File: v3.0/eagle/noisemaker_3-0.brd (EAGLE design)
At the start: 76.3 x 66.7 mm, 58 parts, among them IC1 REG1117, U3 ATMEGA32U4, Y1 16MHz

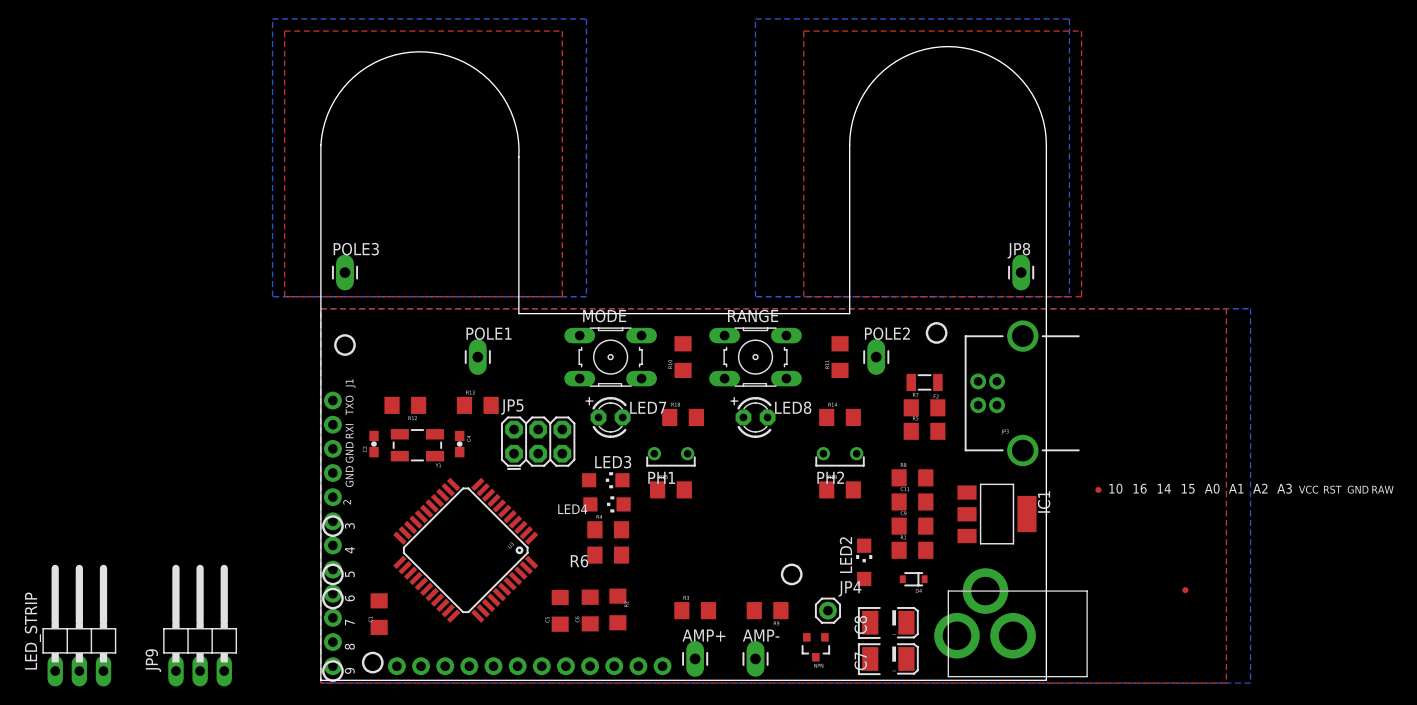
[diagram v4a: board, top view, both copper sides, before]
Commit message: board file
text has been updated, layout is completed. needs logos, names, more text love.
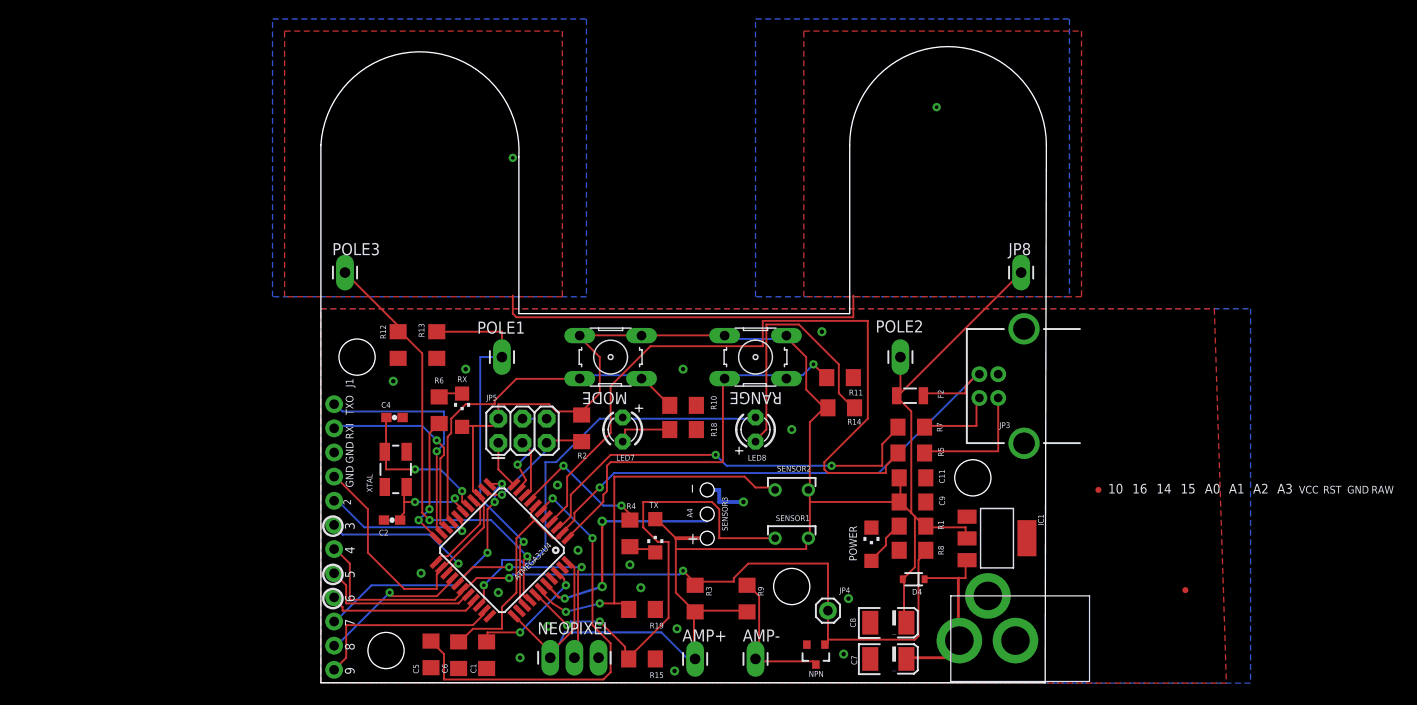
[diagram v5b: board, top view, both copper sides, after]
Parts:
- removed JP6: (no value), SparkFun:1X12
- removed JP9, LED_STRIP: (no value), pinhead:1X03/90
- removed LED2: Red, adafruit:CHIPLED_1206
- removed LED3: Yellow, adafruit:CHIPLED_1206
- removed LED4: Green, adafruit:CHIPLED_1206
- removed PH1, PH2: M9960_11B, photo-elements:M9960
- removed U3: ATMEGA32U4, SparkFun-DigitalIC:SPARKFUN-DIGITALIC_TQFP44
- removed Y1: 16MHz, SparkFun:CRYSTAL-SMD-5X3
- added ATMEGA32U4: ATMEGA32U4, SparkFun-DigitalIC:SPARKFUN-DIGITALIC_TQFP44
- added NEOPIXEL: (no value), SparkFun-Connectors:1X03_LONGPADS
- added POWER: Red, adafruit:CHIPLED_1206
- added RX: Green, adafruit:CHIPLED_1206
- added SENS3: (no value), SparkFun-Connectors:1X03_PP_HOLES_ONLY
- added SENSOR1, SENSOR2: M9960_11B, photo-elements:M9960
- added TX: Yellow, adafruit:CHIPLED_1206
- added XTAL: 16MHz, SparkFun:CRYSTAL-SMD-5X3
- moved R19 24.3 mm to (33.8, 7.75), turned to 180 degrees
- moved R6 23.4 mm to (12.4, 28.7), turned to 90 degrees
- moved R2 19.4 mm to (27.4, 26.8), turned to 90 degrees
- moved R15 18.0 mm to (33.8, 2.54), turned to 180 degrees
- moved C6 14.6 mm to (14.5, 2.94)
- moved C5 14.3 mm to (11.6, 3.02)
- moved C1 12.1 mm to (17.4, 2.94)
- moved C2 8.22 mm to (7.49, 17.1), turned to 180 degrees
- moved R13 7.68 mm to (12.2, 35.6), turned to 270 degrees
- moved R8 7.62 mm to (62.2, 14.0)
- moved C4 7.41 mm to (7.75, 27.9), turned to 0 degrees
- moved R12 6.40 mm to (8.13, 35.6), turned to 90 degrees
- moved R10 5.08 mm to (38.1, 29.2), turned to 180 degrees
- moved R5 2.68 mm to (62.1, 24.2)
- moved IC1 2.54 mm to (71.1, 15.2)
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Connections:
- removed net N$11: LED_STRIP.3
- removed net N$6: LED_STRIP.1
- net A0: now also ATMEGA32U4.36; no longer JP6.8, U3.36
- net A1: now also ATMEGA32U4.37; no longer JP6.7, U3.37
- net A2: now also ATMEGA32U4.38, SENSOR1.2; no longer JP6.6, PH1.2, U3.38
- net A3: now also ATMEGA32U4.39, SENSOR2.2; no longer JP6.5, PH2.2, U3.39
- net A4: now also ATMEGA32U4.40, SENS3.2; no longer JP9.2, U3.40
- net A5: now also ATMEGA32U4.41; no longer U3.41
- net AREF: now also ATMEGA32U4.42; no longer U3.42
- net D+: now also ATMEGA32U4.4; no longer U3.4
- net D-: now also ATMEGA32U4.3; no longer U3.3
- net D10: now also ATMEGA32U4.30, JP7.4; no longer JP6.12, U3.30
- net D11: now also ATMEGA32U4.12, JP7.3; no longer U3.12
- net D12: now also ATMEGA32U4.26, JP7.2; no longer U3.26
- net D13: now also ATMEGA32U4.32, JP7.1; no longer U3.32
- net D14: now also ATMEGA32U4.8; no longer U3.8
- net D2: now also ATMEGA32U4.19; no longer JP7.8, U3.19
- net D3: now also ATMEGA32U4.18, JP7.8; no longer JP7.7, U3.18
- net D4: now also ATMEGA32U4.25, JP7.7; no longer JP7.6, R11.2, RANGE.3, RANGE.4, U3.25
- net D5: now also ATMEGA32U4.31, LED7.A, LED8.K; no longer JP7.5, U3.31
- net D6: now also ATMEGA32U4.27, NEOPIXEL.2; no longer JP7.4, LED_STRIP.2, U3.27
- net D7: now also ATMEGA32U4.1, R11.2, RANGE.3, RANGE.4; no longer JP7.3, LED7.A, LED8.K, U3.1
- net D8: now also ATMEGA32U4.28, JP7.6; no longer JP7.2, U3.28
- net D9: now also ATMEGA32U4.29, JP7.5; no longer JP7.1, U3.29
- net GND: now also ATMEGA32U4.15, ATMEGA32U4.23, ATMEGA32U4.33, ATMEGA32U4.35, ATMEGA32U4.43, ATMEGA32U4.5, NEOPIXEL.3, POWER.C, SENS3.3; no longer JP6.2, JP7.9, JP9.3, LED2.C, U3.15, U3.23, U3.33, U3.35, U3.43, U3.5
- net MISO: now also ATMEGA32U4.11; no longer JP6.10, U3.11
- net MOSI: now also ATMEGA32U4.10; no longer JP6.11, U3.10
- net N$1: now also ATMEGA32U4.16, XTAL.1; no longer U3.16, Y1.1
- net N$10: now also POWER.A; no longer LED2.A
- net N$2: now also ATMEGA32U4.17, XTAL.3; no longer U3.17, Y1.3
- net N$4: now also ATMEGA32U4.6; no longer U3.6
- net N$5: now also TX.C; no longer LED3.C
- net N$7: now also RX.C; no longer LED4.C
- net RAW: no longer JP6.1
- net RESET: now also ATMEGA32U4.13; no longer JP6.3, U3.13
- net RXI: now also ATMEGA32U4.20; no longer U3.20
- net SCK: now also ATMEGA32U4.9; no longer JP6.9, U3.9
- net TXLED: now also ATMEGA32U4.22; no longer U3.22
- net TXO: now also ATMEGA32U4.21; no longer U3.21
- net UVCC: now also ATMEGA32U4.2, ATMEGA32U4.7; no longer U3.2, U3.7
- net VCC: now also ATMEGA32U4.14, ATMEGA32U4.24, ATMEGA32U4.34, ATMEGA32U4.44, JP7.9, NEOPIXEL.1, RX.A, SENS3.1, SENSOR1.1, SENSOR2.1, TX.A; no longer JP6.4, JP9.1, LED3.A, LED4.A, PH1.1, PH2.1, U3.14, U3.24, U3.34, U3.44
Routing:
- net VCC: track 0.00 -> 255.0 mm
- net D8: track 0.00 -> 87.5 mm, vias 0 -> 2
- net UVCC: track 0.00 -> 82.4 mm, vias 0 -> 1
- net D+: track 0.00 -> 75.1 mm
- net A2: track 0.00 -> 50.8 mm, vias 0 -> 2
- net A1: track 0.00 -> 46.9 mm, vias 0 -> 2
- net N$4: track 0.00 -> 45.1 mm, vias 0 -> 2
- net D5: track 0.00 -> 44.5 mm, vias 0 -> 1
- net D-: track 0.00 -> 43.9 mm, vias 0 -> 2
- net D7: track 0.00 -> 43.0 mm, vias 0 -> 1
- net A3: track 0.00 -> 41.7 mm, vias 0 -> 2
- net A0: track 0.00 -> 40.2 mm, vias 0 -> 1
- net N$3: track 0.00 -> 40.2 mm, vias 0 -> 2
- net D2: track 0.00 -> 37.7 mm
- net D11: track 0.00 -> 28.3 mm, vias 0 -> 3
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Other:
- board size 76.3 x 66.7 mm -> 76.3 x 66.9 mm
- board text added: "+"
- board text added: "A4"
- board text added: "SENSOR3"
- board text added: "_"

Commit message: board layout, all text complete. ready for manufacture, RC1
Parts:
- removed U$3: OSHW-LOGOS, SparkFun:OSHW-LOGO-S
- added LOGO1: OSHW-LOGOM, SparkFun-Aesthetics:OSHW-LOGO-M
- moved JP1 93.2 mm to (2.03, 37.7)
- moved JP2 7.62 mm to (74.2, 20.3)
- moved SENSOR1 2.16 mm to (47.4, 15.2)
- moved SENSOR2 2.16 mm to (47.4, 20.3)
- moved JP4 1.91 mm to (51.8, 6.48)
- renumbered JP5 to ICSP, LED7 to LED1, LED8 to LED2, POWER to PWR
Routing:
- net N$3: track 40.2 -> 0.00 mm, vias 2 -> 0
- net A2: track 50.8 -> 33.4 mm
- net VCC: track 255.0 -> 265.0 mm
- net D+: track 75.1 -> 68.3 mm
- net A0: track 40.2 -> 43.5 mm
- net A3: track 41.7 -> 39.7 mm
- net D8: track 87.5 -> 86.5 mm
- net GND: track 14.7 -> 13.8 mm
- added copper zone on layer 1, net A1
- added copper zone on layer 16, net A1
- added copper zone on layer 1, net VCC
- added copper zone on layer 16, net VCC
- removed copper zone on layer 1, net N$3
- removed copper zone on layer 16, net N$3
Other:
- board text added: "11"
- board text added: "12"
- board text added: "13"
- board text added: "5V"
- board text added: "L.Campbell J.Brucker-Cohen K.Moriwaki J.McDonald T.Gou N.Messier T.Wen J.Saavedra"
- board text added: "USB"
- board text added: "gadgIteration"
- board text added: "gadgiteration.org"
- board text added: "noisemaker"
- board text added: "open hardware"
- board text added: "v3.0"
- board text removed: "14"
- board text removed: "15"
- board text removed: "16"
- board text removed: "2"
- board text removed: "5"
- board text removed: "6"
- board text removed: "7"
- board text removed: "A0"
- board text removed: "A1"
- board text removed: "A2"
- board text removed: "A3"
- board text removed: "J1"
- board text removed: "RAW"
- board text removed: "RST"
- board text removed: "VCC"
